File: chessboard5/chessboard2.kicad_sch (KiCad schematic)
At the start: 18 parts, among them J1 IN, J2 OUT, J3 IN, J4 OUT, Q1 AO3401A, U1 TMAG5273, U2 WS2814F

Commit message: update slightly
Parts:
- removed D2, D3, D4: Vf=.6, symbol Device:D
- added C1: 10u, Capacitor_SMD:C_0603_1608Metric_Pad1.08x0.95mm_HandSolder, symbol Device:C
- C2: value 10u -> 1u
- D1, D5, D6, R1, R2, R4: footprint (none) -> Capacitor_SMD:C_0603_1608Metric_Pad1.08x0.95mm_HandSolder
- Q1: footprint Package_TO_SOT_SMD:SOT-23 -> Package_TO_SOT_SMD:SOT-23_Handsoldering
- U1: footprint Package_TO_SOT_SMD:SOT-23-6 -> Package_TO_SOT_SMD:SOT-23-6_Handsoldering
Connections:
- net 5V: now also C1.1; no longer Q1.3 (D), R3.2
- net GND: now also C1.2
- net +3V3: now reaches Q1.2 (S)
- net +3V3: now also R3.2
- net at C2.1, U1.4 (VDD): now also Q1.3 (D)

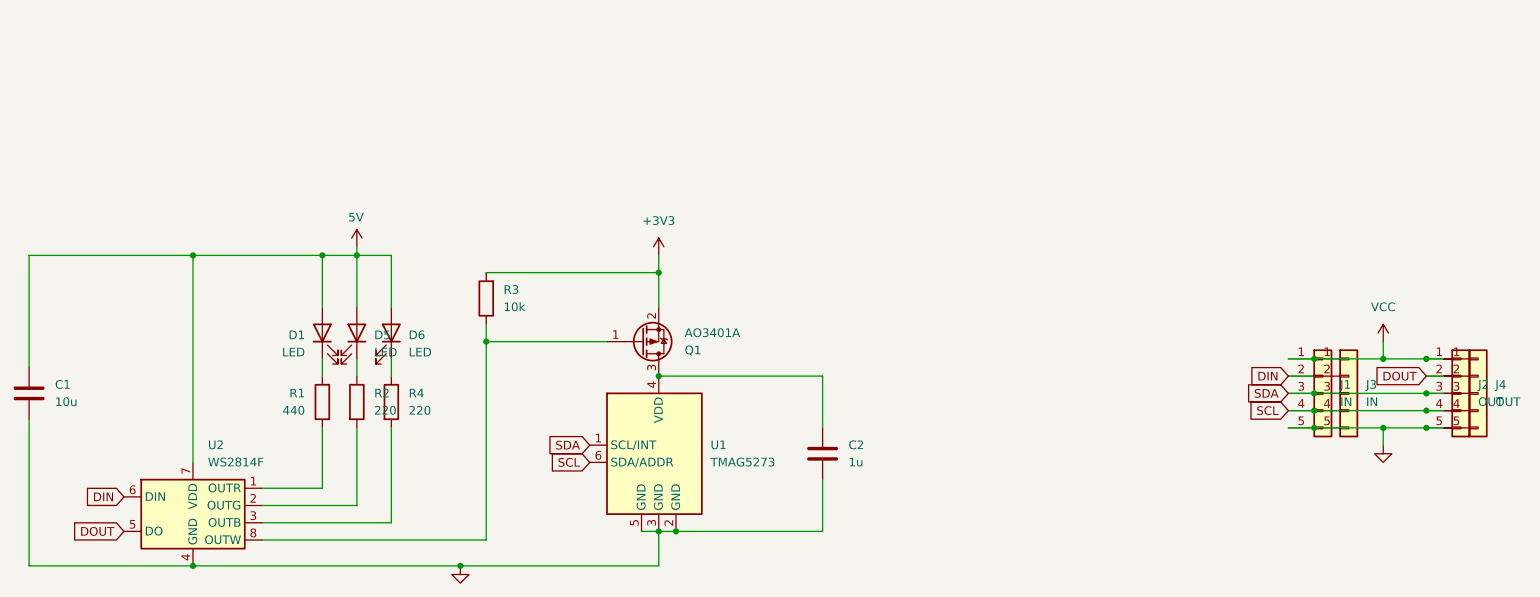
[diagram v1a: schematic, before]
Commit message: fix up schematic for chessboard5
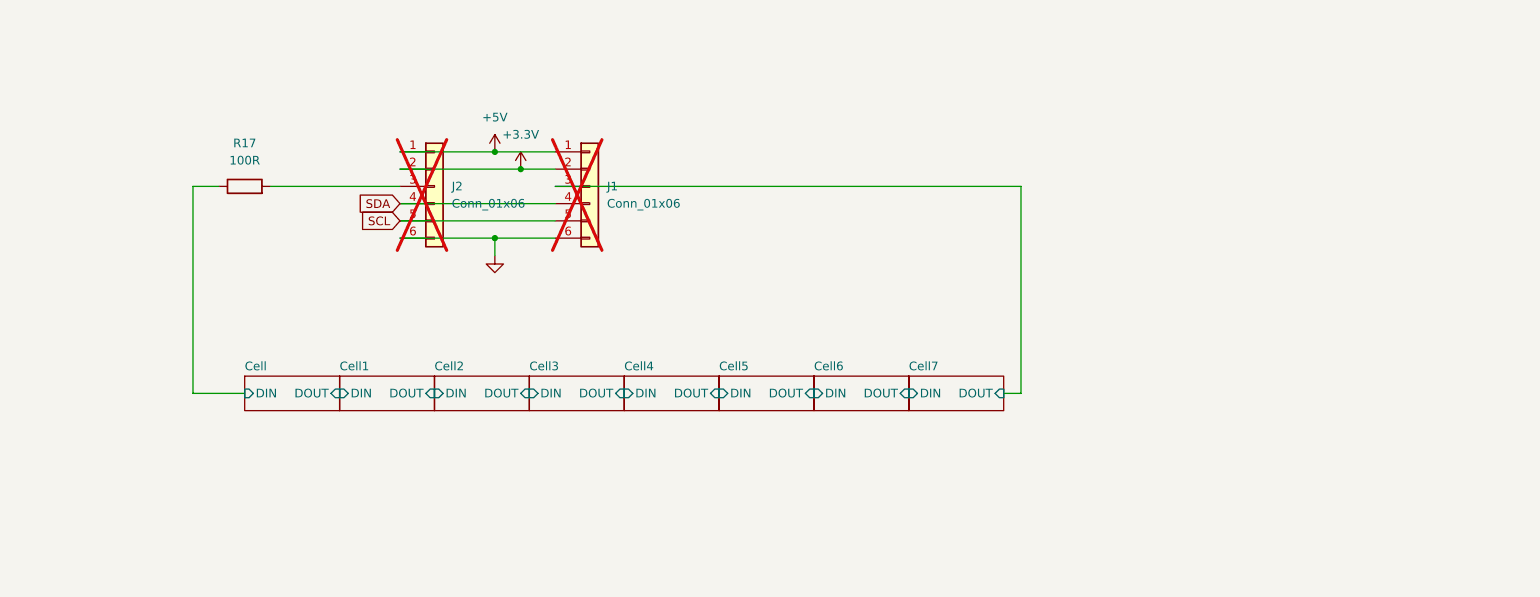
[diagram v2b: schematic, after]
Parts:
- removed C1: 10u, Capacitor_SMD:C_0603_1608Metric_Pad1.08x0.95mm_HandSolder, symbol Device:C
- removed C2: 1u, Capacitor_SMD:C_0603_1608Metric_Pad1.08x0.95mm_HandSolder, symbol Device:C
- removed D1, D5, D6: LED, Capacitor_SMD:C_0603_1608Metric_Pad1.08x0.95mm_HandSolder, symbol Device:LED
- removed J1, J3: IN, Connector_PinSocket_2.54mm:PinSocket_1x05_P2.54mm_Vertical, symbol Connector_Generic:Conn_01x05
- removed J2, J4: OUT, Connector_PinHeader_2.54mm:PinHeader_1x05_P2.54mm_Vertical, symbol Connector_Generic:Conn_01x05
- removed Q1: AO3401A, Package_TO_SOT_SMD:SOT-23_Handsoldering, symbol Transistor_FET:AO3401A
- removed R1: 440, Capacitor_SMD:C_0603_1608Metric_Pad1.08x0.95mm_HandSolder, symbol Device:R
- removed R2, R4: 220, Capacitor_SMD:C_0603_1608Metric_Pad1.08x0.95mm_HandSolder, symbol Device:R
- removed R3: 10k, Resistor_SMD:R_0603_1608Metric_Pad0.98x0.95mm_HandSolder, symbol Device:R
- removed U1: TMAG5273, Package_TO_SOT_SMD:SOT-23-6_Handsoldering, symbol Sensor_Magnetic:TLV493D
- removed U2: WS2814F, Package_TO_SOT_SMD:SOT-23-8_Handsoldering, symbol Driver_LED:WS2811
- added J1, J2: Conn_01x06, symbol Connector_Generic:Conn_01x06
- added R17: 100R, Resistor_SMD:R_0603_1608Metric_Pad0.98x0.95mm_HandSolder, symbol Device:R
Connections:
- net GND: now also J1.6 (Pin_6), J2.6 (Pin_6)
- net SCL: now also J1.5 (Pin_5), J2.5 (Pin_5)
- net SDA: now also J1.4 (Pin_4), J2.4 (Pin_4)
- new net: J2.3 (Pin_3), R17.2
- new net +3.3V: J1.2 (Pin_2), J2.2 (Pin_2)
- new net +5V: J1.1 (Pin_1), J2.1 (Pin_1)
- new net Cell/DIN: R17.1
- new net Cell7/DOUT: J1.3 (Pin_3)
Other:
- added sheet Cell (cell.kicad_sch)
- added sheet Cell1 (cell.kicad_sch)
- added sheet Cell2 (cell.kicad_sch)
- added sheet Cell3 (cell.kicad_sch)
- added sheet Cell4 (cell.kicad_sch)
- added sheet Cell5 (cell.kicad_sch)
- added sheet Cell6 (cell.kicad_sch)
- added sheet Cell7 (cell.kicad_sch)

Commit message: Progress!!!
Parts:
- J1, J2: footprint (none) -> Connector_IDC:IDC-Header_2x03_P2.54mm_Vertical
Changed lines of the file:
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@@
 			)
 		)
-		(property "Footprint" ""
+		(property "Footprint" "Connector_IDC:IDC-Header_2x03_P2.54mm_Vertical"
 			(at 132.08 96.52 0)
 			(effects
@@
 			)
 		)
-		(property "Footprint" ""
+		(property "Footprint" "Connector_IDC:IDC-Header_2x03_P2.54mm_Vertical"
 			(at 154.94 96.52 0)
 			(effects

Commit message: finished chessboard v5!!!
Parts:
- added H1: MountingHole, MountingHole:MountingHole_3.2mm_M3, symbol Mechanical:MountingHole
- J1, J2: footprint Connector_IDC:IDC-Header_2x03_P2.54mm_Vertical -> Connector_PinHeader_2.54mm:PinHeader_2x03_P2.54mm_Vertical

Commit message: fix chessboard5 for ordering;
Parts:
- added JP1, JP2: SolderJumper_3_Open, Jumper:SolderJumper-3_P1.3mm_Open_RoundedPad1.0x1.5mm, symbol Jumper:SolderJumper_3_Open
- H1: now not fitted
- R17: got (none) -> RC0603FR-07100RL; gotnum (none) -> 1000
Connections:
- net at J2.3 (Pin_3): now also JP1.2 (C); no longer R17.2
- net Cell7/DOUT: no longer names the net of J1.3 (Pin_3)
- net Cell7/DOUT: now also JP2.2 (C)
- new net DIN_G: JP1.1 (A), JP2.1 (A), R17.2
- new net DOUT_G: JP1.3 (B), JP2.3 (B)
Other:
- moved on the sheet: R17
